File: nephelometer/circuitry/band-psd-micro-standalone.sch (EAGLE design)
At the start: 59 parts, among them IC1 LMC6484P, IC2 LM555N, IC3 74HCT74N, IC4 4044N, T1 2N2222, T2 2N2222, U1 MAX4544, U4 MotA

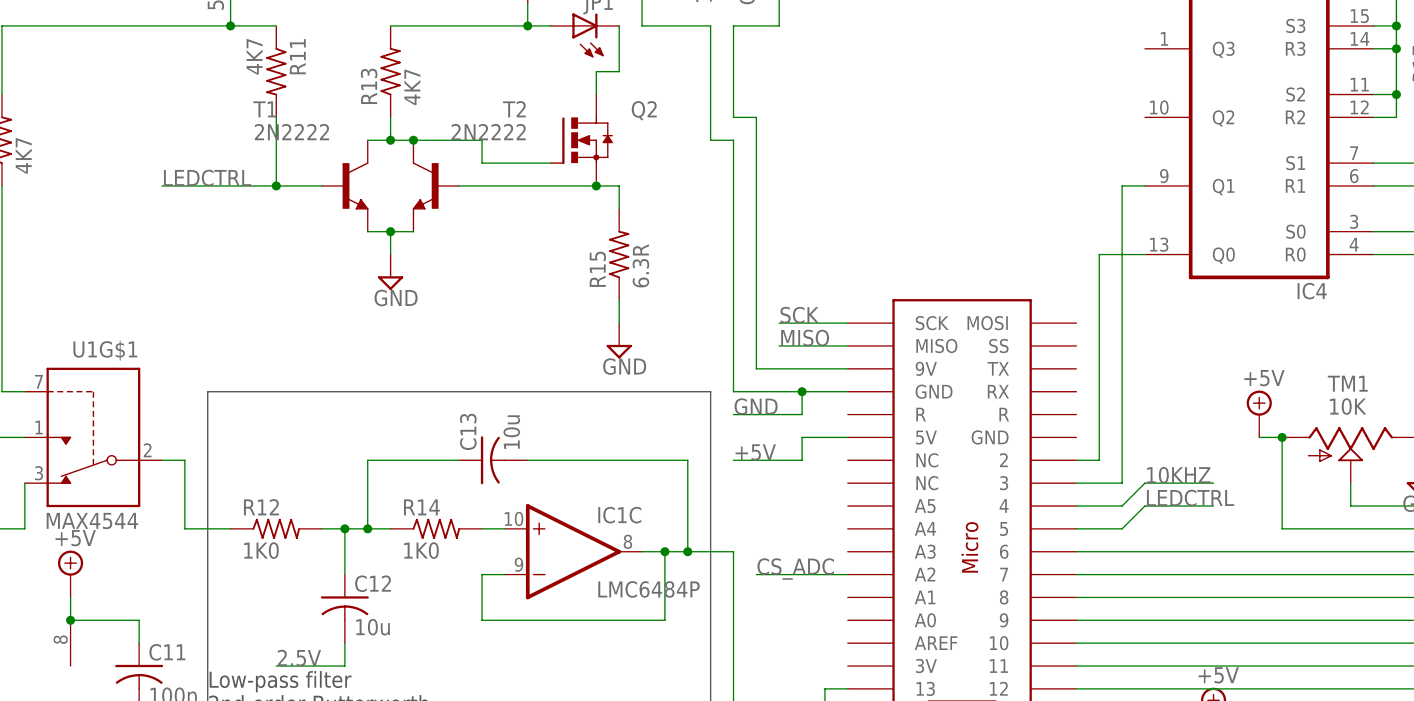
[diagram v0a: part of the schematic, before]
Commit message: Fixed a minor flaw in which Arduino input pin is connected on the wrong side of the base resistor of the LED control and so never reads positive
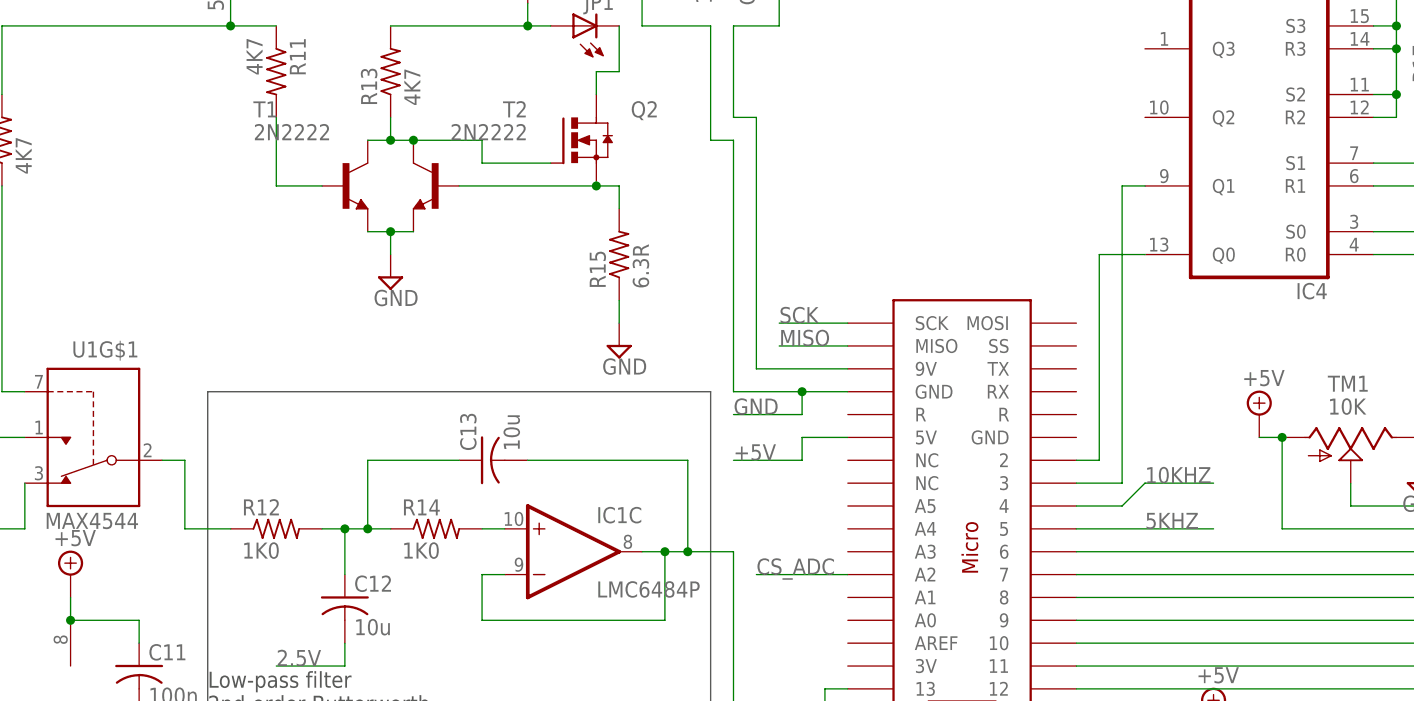
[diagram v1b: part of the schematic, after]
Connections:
- net 5KHZ: now also U3.5
- net LEDCTRL: no longer U3.5
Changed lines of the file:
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@@
 <?xml version="1.0" encoding="utf-8"?>
 <!DOCTYPE eagle SYSTEM "eagle.dtd">
-<eagle version="7.1.0">
+<eagle version="7.0.0">
 <drawing>
 <settings>
@@
 <pinref part="T1" gate="G$1" pin="B"/>
 <wire x1="157.48" y1="73.66" x2="162.56" y2="73.66" width="0.1524" layer="91"/>
-<wire x1="157.48" y1="73.66" x2="144.78" y2="73.66" width="0.1524" layer="91"/>
-<junction x="157.48" y="73.66"/>
-<label x="144.78" y="73.66" size="1.778" layer="95"/>
-</segment>
-<segment>
-<pinref part="U3" gate="G$1" pin="5"/>
-<wire x1="246.38" y1="35.56" x2="251.46" y2="35.56" width="0.1524" layer="91"/>
-<wire x1="251.46" y1="35.56" x2="254" y2="38.1" width="0.1524" layer="91"/>
-<wire x1="254" y1="38.1" x2="261.62" y2="38.1" width="0.1524" layer="91"/>
-<label x="254" y="38.1" size="1.778" layer="95"/>
 </segment>
 </net>
@@
 <label x="149.86" y="99.06" size="1.778" layer="95" rot="R270"/>
 </segment>
-</net>
+<segment>
+<pinref part="U3" gate="G$1" pin="5"/>
+<wire x1="246.38" y1="35.56" x2="261.62" y2="35.56" width="0.1524" layer="91"/>
+<label x="254" y="35.56" size="1.778" layer="95"/>
+</segment>
+</net>

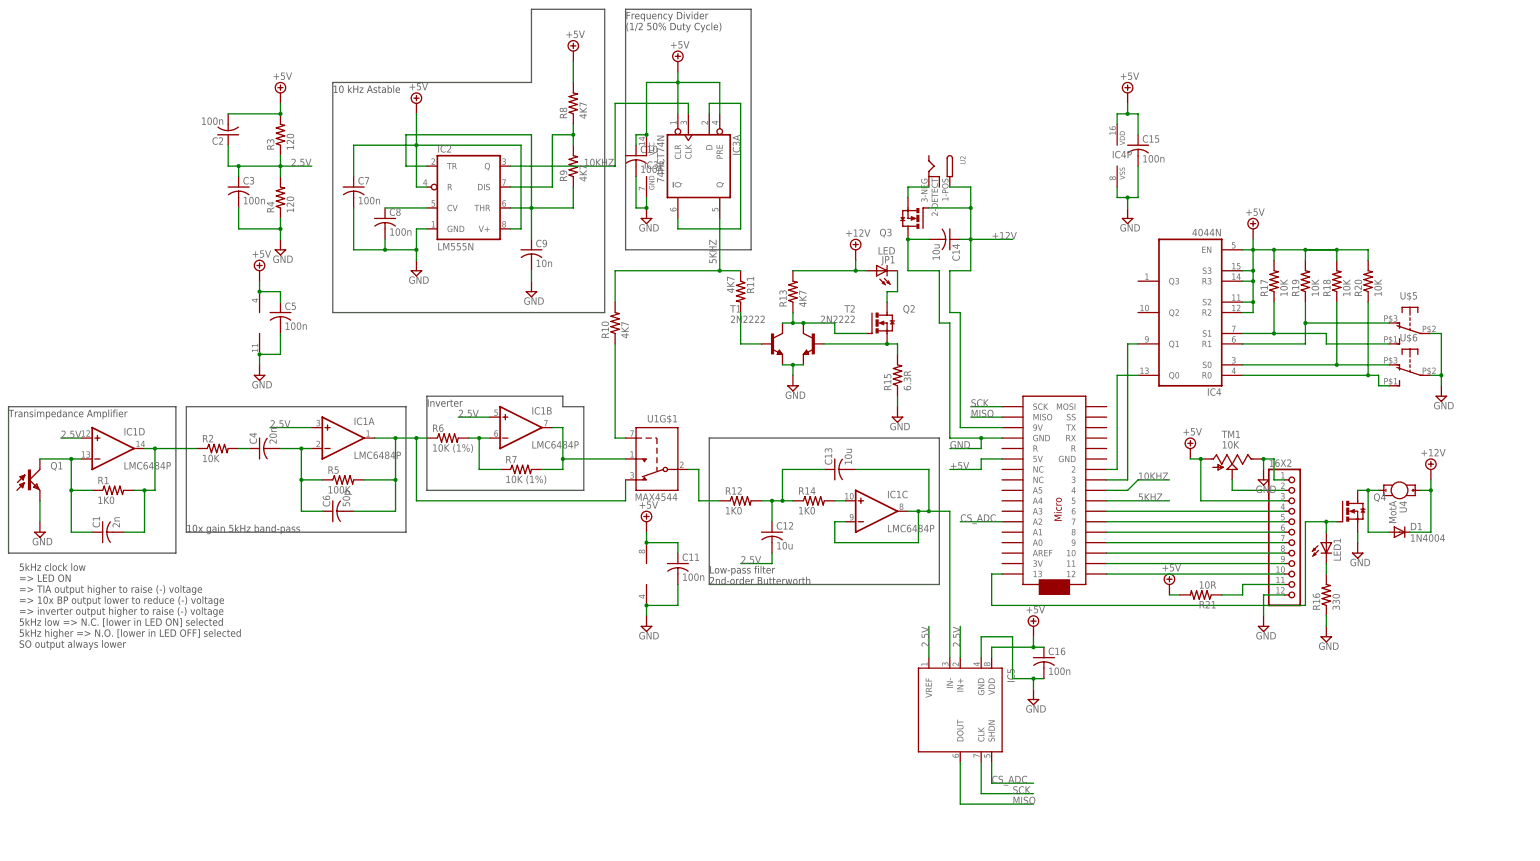
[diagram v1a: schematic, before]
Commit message: Enlarged board, included 5V regulator on board, more decoupling, 4 buttons on 4 PCIO pins
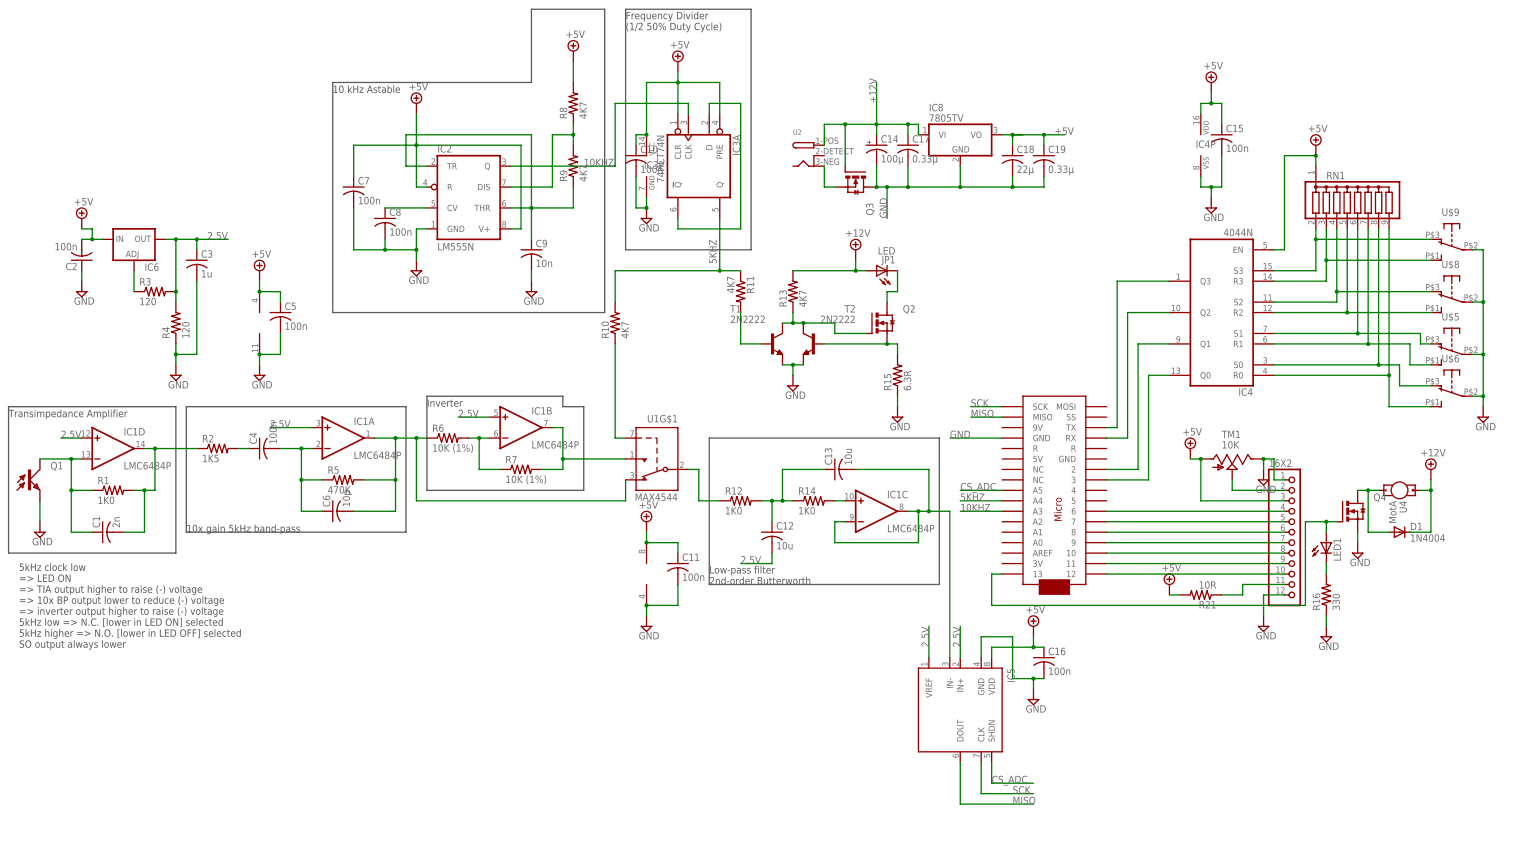
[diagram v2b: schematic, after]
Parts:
- removed R17, R18, R19, R20: 10K, adafruit:R-US_0204/2V
- added C17, C19: 0.33µ, adafruit:C-US025-025X050
- added C18: 22µ, adafruit:C-US050-045X075
- added IC6: (no value), v-reg:LM317L
- added IC8: 7805TV, linear:7805TV
- added RN1: (no value), resistor-sil:G08R
- added U$8, U$9: (no value), ingolia:APE1F-5M-10-Z
- C14: value 10u -> 100µ; device adafruit:C-US050-050X075 -> adafruit:CPOL-USE2.5-7
- C3: value 100n -> 1u
- C4: value 20n -> 100n
- C6: value 50p -> 10p
- R2: value 10K -> 1K5
- R5: value 100K -> 470K
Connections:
- new net N$35: IC6.ADJ, R3.1
- new net N$39: IC4A.Q3, U3.TX
- new net N$40: IC4A.R1, RN1.7, U$5.NO
- new net N$42: IC4A.S0, RN1.8, U$6.NC
- new net N$43: IC4A.R0, RN1.9, U$6.NO
- new net N$44: IC4A.S1, RN1.6, U$5.NC
- new net N$45: IC4A.Q2, U3.RX
- net +12V: now also C14.+, C17.1, IC8.VI; no longer C14.1, U3.9V
- net +5V: now also C18.1, C19.1, IC6.IN, IC8.VO, RN1.1; no longer IC4A.R2, IC4A.R3, IC4A.S2, IC4A.S3, R17.2, R18.2, R19.2, R20.2, R3.2, U3.5V
- net 10KHZ: now also U3.A3; no longer U3.4
- net 2.5V: now also IC6.OUT, R3.2; no longer C2.1, R3.1
- net 5KHZ: now also U3.A4; no longer U3.5
- net CS_ADC: now also U3.A5; no longer U3.A2
- net GND: now also C14.-, C17.2, C18.2, C19.2, C2.1, U$8.COM, U$9.COM; no longer C14.2
- net N$31: now also IC4A.Q0; no longer IC4A.Q1
- net N$32: now also IC4A.Q1; no longer IC4A.Q0
- net N$33: now also IC4A.S3, RN1.2, U$9.NC; no longer IC4A.S1, R17.1, U$5.NO
- net N$34: now also IC4A.R3, RN1.3, U$9.NO; no longer IC4A.R1, R19.1, U$5.NC
- net N$36: now also IC4A.S2, RN1.4, U$8.NC; no longer IC4A.S0, R18.1, U$6.NC
- net N$37: now also IC4A.R2, RN1.5, U$8.NO; no longer IC4A.R0, R20.1, U$6.NO
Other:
- moved on the sheet: C15, C2, C3, IC4, IC4P, Q3, R3, R4, U$5, U$6, U2

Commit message: Fixed up filter design -- topology of high-gain bandpass and component values for low-pass
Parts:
- C12: value 10u -> 22nF
- C13: value 10u -> 50nF
- R12: value 1K0 -> 330K
- R14: value 1K0 -> 680K
- R2: value 1K5 -> 1K0
- R5: value 470K -> 330K
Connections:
- removed net N$11: 16X2.4, U3.6
- removed net N$15: 16X2.5, U3.7
- removed net N$20: 16X2.6, U3.8
- removed net N$21: 16X2.7, U3.9
- removed net N$24: 16X2.8, U3.10
- removed net N$29: 16X2.9, U3.11
- removed net N$30: 16X2.10, U3.12
- net 2.5V: now also R3.1; no longer R3.2, R4.2
- net N$2: now also C4.2, R2.1; no longer C4.1, R2.2
- net N$22: now also C4.1; no longer R2.1
- net N$25: now also R2.2; no longer C4.2
- net N$35: now also R3.2, R4.2; no longer R3.1
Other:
- note added: "1.6 kHz"
- note added: "48 kHz"
- moved on the sheet: C3, C4, C6, R2, R3, R4

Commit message: Better wiring for push-buttons (to PCINT pins) and LCD (allow INT)
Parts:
- added JP2: (no value), pinhead:PINHD-1X2
- 16X2: value (none) -> PINHD-1X10; device adafruit:PINHD-1X12-CB -> adafruit:PINHD-1X10
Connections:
- new net N$11: IC4A.Q1, U3.11
- new net N$15: IC4A.Q0, U3.12
- new net N$21: JP2.1, R21.1
- new net N$24: 16X2.10, U3.8
- new net N$29: 16X2.9, U3.7
- new net N$30: 16X2.8, U3.6
- new net N$46: 16X2.4, U3.2
- net GND: now also JP2.2; no longer 16X2.12
- net N$31: now also 16X2.7, U3.5; no longer IC4A.Q0, U3.3
- net N$32: now also 16X2.6, U3.4; no longer IC4A.Q1, U3.2
- net N$39: now also U3.9; no longer U3.TX
- net N$41: now also 16X2.5, U3.3; no longer 16X2.11, R21.1
- net N$45: now also U3.10; no longer U3.RX
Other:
- moved on the sheet: C15, D1, IC4, IC4P, LED1, Q4, R16, R21, RN1, TM1, U$5, U$6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

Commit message: Started routing power supply
Started part numbers for filter components
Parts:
- C1: value 2n -> 2.2nF; device adafruit:C-US025-025X050 -> adafruit:C-US025-024X044; DIGIKEY# (none) -> BC1029CT-ND; MANF (none) -> Vishay BC Components; MANF# (none) -> K222J15C0GF5TL2
- C4: device adafruit:C-US025-025X050 -> adafruit:C-US025-060X050; DIGIKEY# (none) -> 445-8325-ND; MANF (none) -> TDK Corporation; MANF# (none) -> FK16C0G1H104J
- C6: device adafruit:C-US025-025X050 -> adafruit:C-US025-024X044; DIGIKEY# (none) -> BC1001CT-ND; MANF (none) -> Vishay BC Components; MANF# (none) -> K100J15C0GF5TL2
- Q1: device ingolia:LTR-4206PTRANS -> ingolia:LTR-4206
- R1, R2: device adafruit:R-US_0204/2V -> adafruit:R-US_0204/5; DIGIKEY# (none) -> S1KCACT-ND; MANF (none) -> Stackpole Electronics Inc; MANF# (none) -> RNMF14FTC1K00
- R5: device adafruit:R-US_0204/2V -> adafruit:R-US_0309/V; DIGIKEY# (none) -> RNV14FAL330KCT-ND; MANF (none) -> Stackpole Electronics Inc; MANF# (none) -> RNV14FAL330K
- U2: device ingolia:DC-IN-PANEL -> ingolia:DC-IN-PANEL-NODETECT
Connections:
- net GND: now also IC8.GND

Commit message: Specific parts for all analog components
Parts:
- C12: device adafruit:C-US050-025X075 -> adafruit:C-US025-024X044; DIGIKEY# (none) -> 445-8280-ND; MANF (none) -> TDK Corporation; MANF# (none) -> FK14C0G1H223J
- C13: value 50nF -> 47nF; device adafruit:C-US050-025X075 -> adafruit:C-US025-040X050; DIGIKEY# (none) -> 445-8327-ND; MANF (none) -> TDK Corporation; MANF# (none) -> FK16C0G1H473J
- C2: value 100n -> 100nF; DIGIKEY# (none) -> BC1084CT-ND; MANF (none) -> Vishay BC Components; MANF# (none) -> K104K15X7RF5TL2
- C3: device adafruit:C-US025-025X050 -> adafruit:C-US050-024X044; DIGIKEY# (none) -> 445-8614-ND; MANF (none) -> TDK Corporation; MANF# (none) -> FK28X7R1C105K
- C4, C5: value 100n -> 100nF
- C6: value 10p -> 10pF
- IC1: DIGIKEY# (none) -> LMC6484AIN/NOPB-ND; MANF (none) -> Texas Instruments; MANF# (none) -> LMC6484AIN/NOPB
- IC5: DIGIKEY# (none) -> MCP3301-BI/P-ND; MANF (none) -> Microchip Technology; MANF# (none) -> MCP3301-BI/P
- IC6: DIGIKEY# (none) -> 296-33312-5-ND; MANF (none) -> Texas Instruments; MANF# (none) -> LM317LCLP
- R12: DIGIKEY# (none) -> RNV14FAL330KCT-ND; MANF (none) -> Stackpole Electronics Inc; MANF# (none) -> RNV14FAL330K
- R14: DIGIKEY# (none) -> S680KCACT-ND; MANF (none) -> Stackpole Electronics Inc; MANF# (none) -> RNMF14FTC680K
- R3, R4: DIGIKEY# (none) -> S120CACT-ND; MANF (none) -> Stackpole Electronics Inc; MANF# (none) -> RNMF14FTC120R
- R6, R7: DIGIKEY# (none) -> S10KCACT-ND; MANF (none) -> Stackpole Electronics Inc; MANF# (none) -> RNMF14FTC10K0
- U1: DIGIKEY# (none) -> MAX4544CPA+-ND; MANF (none) -> Maxim Integrated; MANF# (none) -> MAX4544CPA+

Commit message: Routed most of board except push-buttons and latch
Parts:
- C14: value 100µ -> 220µF; device adafruit:CPOL-USE2.5-7 -> adafruit:CPOL-USE3.5-8; DIGIKEY# (none) -> P5166-ND; MANF (none) -> Panasonic Electronic Components; MANF# (none) -> ECA-1VM221
- C15, C5, C7: DIGIKEY# (none) -> BC1084CT-ND
- C17, C19: device adafruit:C-US025-025X050 -> adafruit:C-US025-050X050; DIGIKEY# (none) -> 445-5312-ND; MANF (none) -> TDK Corporation; MANF# (none) -> FK14X7R1H334K
- C18: DIGIKEY# (none) -> 445-8455-ND; MANF (none) -> TDK Corporation; MANF# (none) -> FK20X7R1C226M
- D1: value 1N4004 -> 1N4935; DIGIKEY# (none) -> 1N4935FSCT-ND; MANF (none) -> Fairchild Semiconductor; MANF# (none) -> 1N4935
- IC8: DIGIKEY# (none) -> LM7805CT-ND; MANF (none) -> Fairchild Semiconductor; MANF# (none) -> LM7805CT
- Q3, Q4: DIGIKEY# (none) -> IRLB8721PBF-ND; MANF (none) -> International Rectifier; MANF# (none) -> IRLB8721PBF
- R6, R7: device adafruit:R-US_0204/2V -> adafruit:R-US_0204/5
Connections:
- net +5V: now also IC3B.CLK, IC3B.CLR, IC3B.D, IC3B.PRE
- net N$33: now also RN1.3; no longer RN1.2
- net N$34: now also RN1.2; no longer RN1.3
- net N$36: now also RN1.5; no longer RN1.4
- net N$37: now also RN1.4; no longer RN1.5
- net N$40: now also RN1.6; no longer RN1.7
- net N$42: now also RN1.9; no longer RN1.8
- net N$43: now also RN1.8; no longer RN1.9
- net N$44: now also RN1.7; no longer RN1.6
